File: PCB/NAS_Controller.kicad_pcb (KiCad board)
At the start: 4 copper layers, 119.5 x 99.6 mm, 1052 parts, among them J1 Barrel_Jack, J10 Conn_01x10, J11 10103594-0001LF, J12 Conn_01x03, J13 Conn_01x03, J14 20021121-00020C4LF, J15 Conn_01x03, J16 Conn_01x03, J17 Conn_01x03, J18 M20-9990246, J19 Conn_01x03, J2 Conn_01x04, J20 Conn_01x03, J3 105133-0011, J4 10103594-0001LF, J5 NPPN101BFCN-RC, J6 NPPN101BFCN-RC, J7 Conn_01x03, J8 PPTC081LFBN-RC, J9 PPTC081LFBN-RC, Q1 DMN6068LK3-13, Q10 AOD409, Q11 DMG1026UV-7, Q12 DMN6068LK3-13, Q13 DMN6068LK3-13, Q2 DMN6068LK3-13, Q3 MMBT3904-TP, Q4 2N7002, Q5 2N7002, Q6 2N7002, Q7 DMN6068LK3-13, Q8 AOD409, Q9 AOD409, SW1 EG2322, U1 ZXCT1110, U10 TS5A3357DCUR, U11 PCA6416APW,118, U12 ZXGD3009E6TA, U13 TS462CDT, U14 AP65211AWU-7, U15 RT7258GSP, U16 RT7258GSP, U17 LM3481MM, U18 TS462CDT, U19 TS5A3357DCUR, U2 TS462CDT, U3 AZ1084CD-3.3, U4 TS462CDT, U5 TS462CDT, U6 TMS320F28035PAGS, U7 MB85RS16, U8 CY7C65634-48AXCT, U9 TS5A3357DCUR, Y1 12MHz

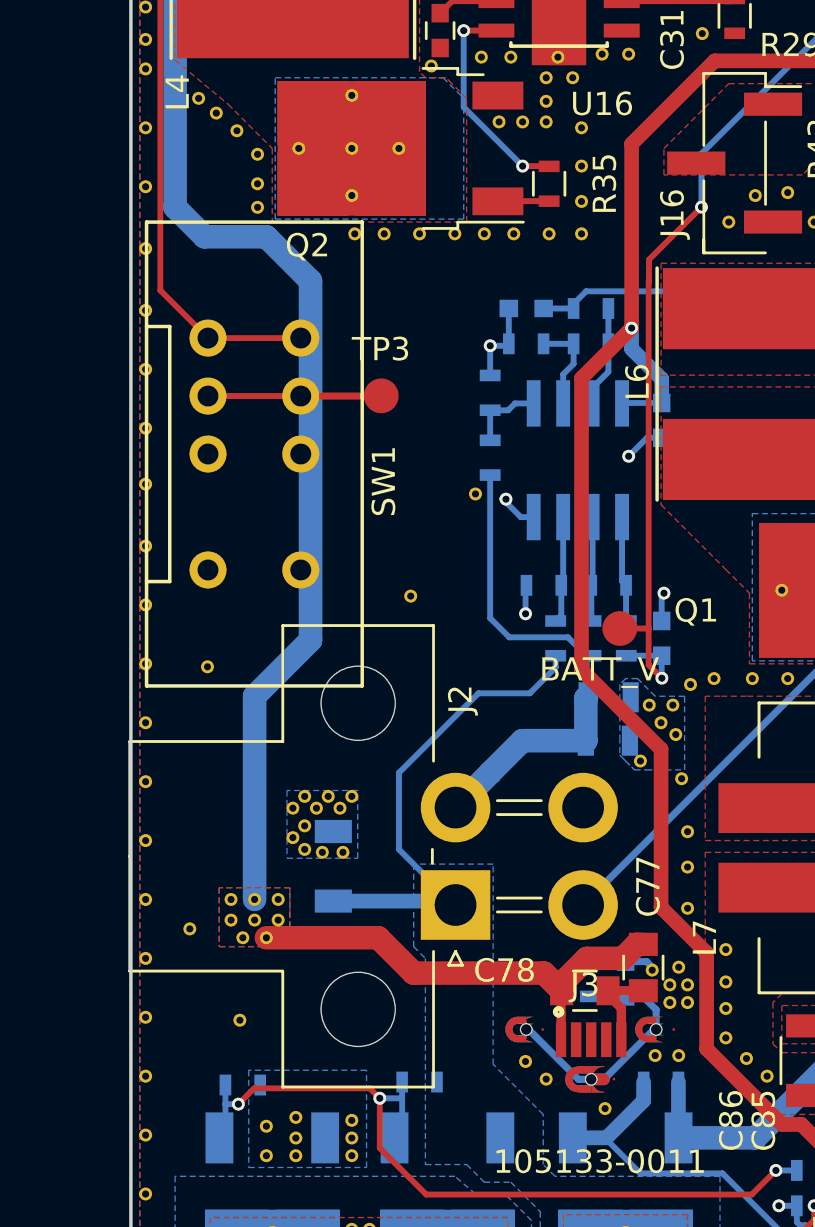
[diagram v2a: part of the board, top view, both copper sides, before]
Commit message: Layout update, need to update USB connector footprint
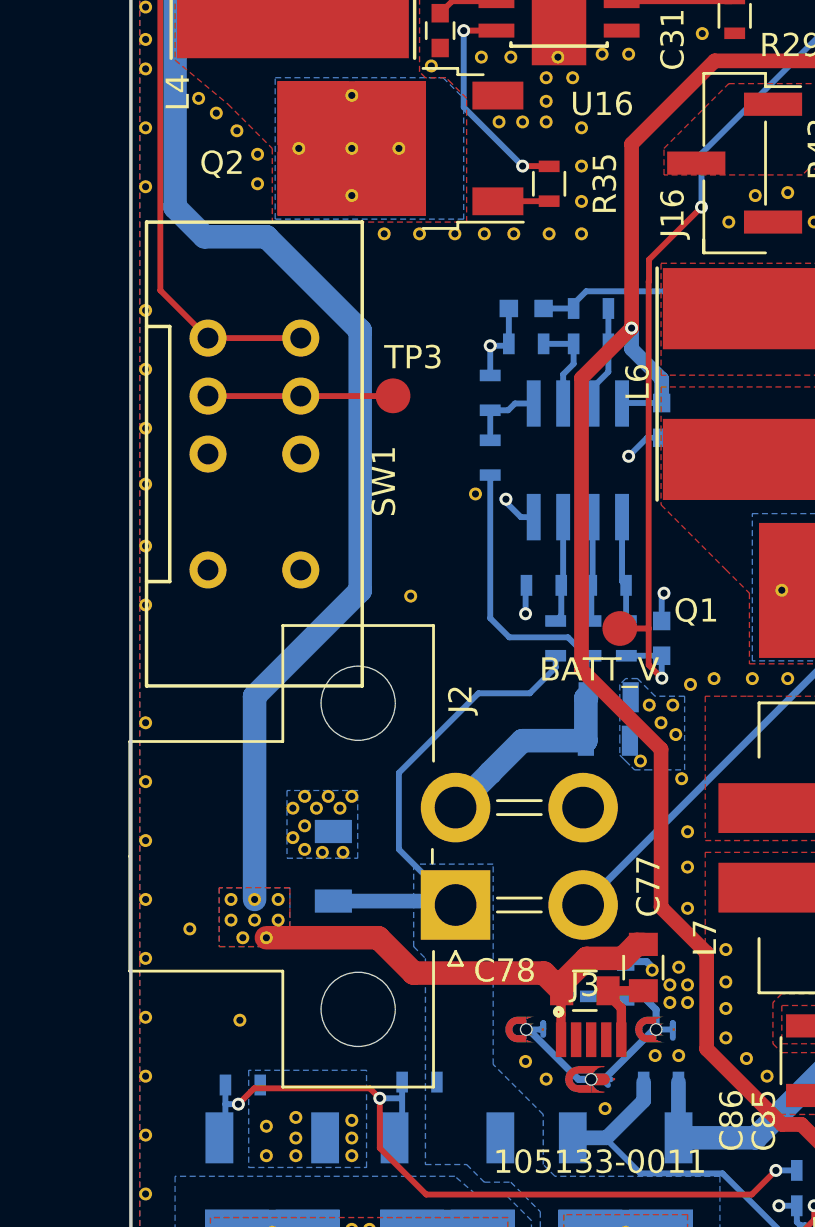
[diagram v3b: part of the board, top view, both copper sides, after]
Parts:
- removed the REF** at (9.65, 37.3)
- removed the REF** at (5.46, 36.2)
- removed the REF** at (3.30, 56.0)
- removed the REF** at (0.64, 55.9)
- removed the REF** at (0.64, 38.0)
- moved TP3 0.51 mm to (11.3, 44.3)
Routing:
- net Net-(C79-Pad2): track 11.3 -> 14.9 mm
- net Net-(C77-Pad1): track 77.0 -> 78.8 mm
- net Net-(SW1-Pad2): track 7.47 -> 8.00 mm

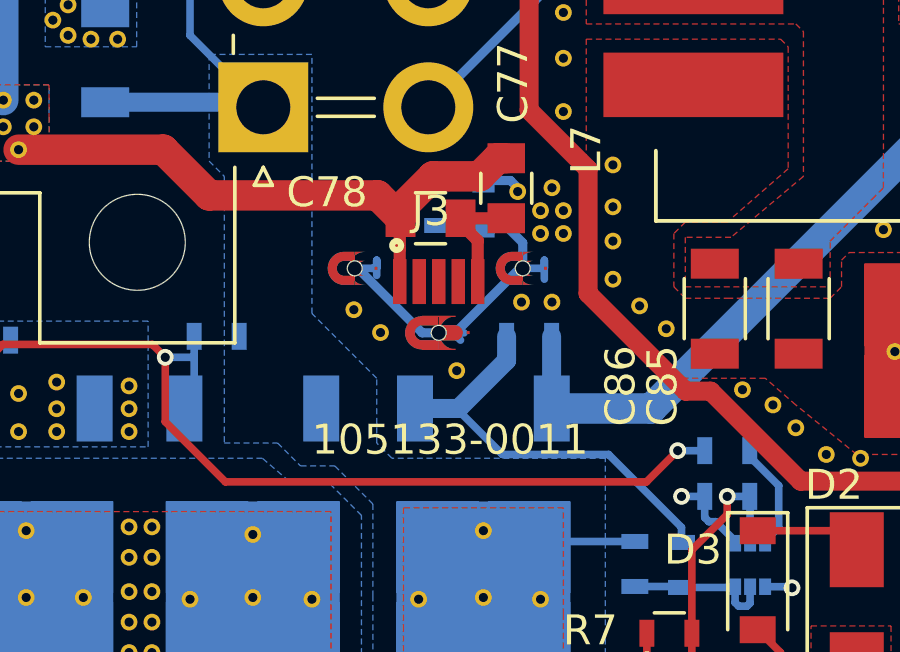
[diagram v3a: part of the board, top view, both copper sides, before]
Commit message: Final rev02 PCB and prep firmware for first load with pinout changes.
PCB: Updated to final gerbers
Firmware: Updated PWM frequency and duty cycles... Changed EPWM1 from 1A to 1B for ELOAD... GPIO config: removed PWM from GPIO0, added it to GPIO1, and configured GPIO30 for ELOAD_SEL.
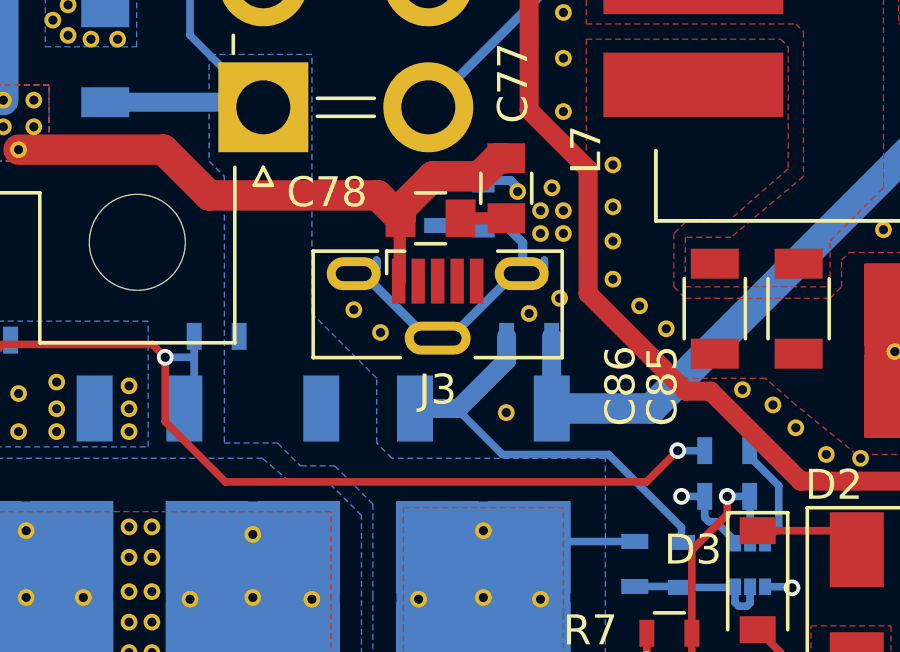
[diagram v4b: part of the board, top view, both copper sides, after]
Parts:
- J3: footprint 105133-0011:MOLEX_105133-0011 -> Connectors_USB:USB_Micro-B_Vertical_Molex-105133-0001
- moved REF** 2.16 mm to (22.1, 76.5)
- moved J3 1.25 mm to (19.8, 72.9)
- moved REF** 0.46 mm to (22.9, 73.2)
- moved REF** 0.28 mm to (23.9, 72.6)
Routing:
- net GND: track 208.3 -> 206.1 mm
